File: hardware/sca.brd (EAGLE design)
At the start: 194.3 x 73.3 mm, 31 parts

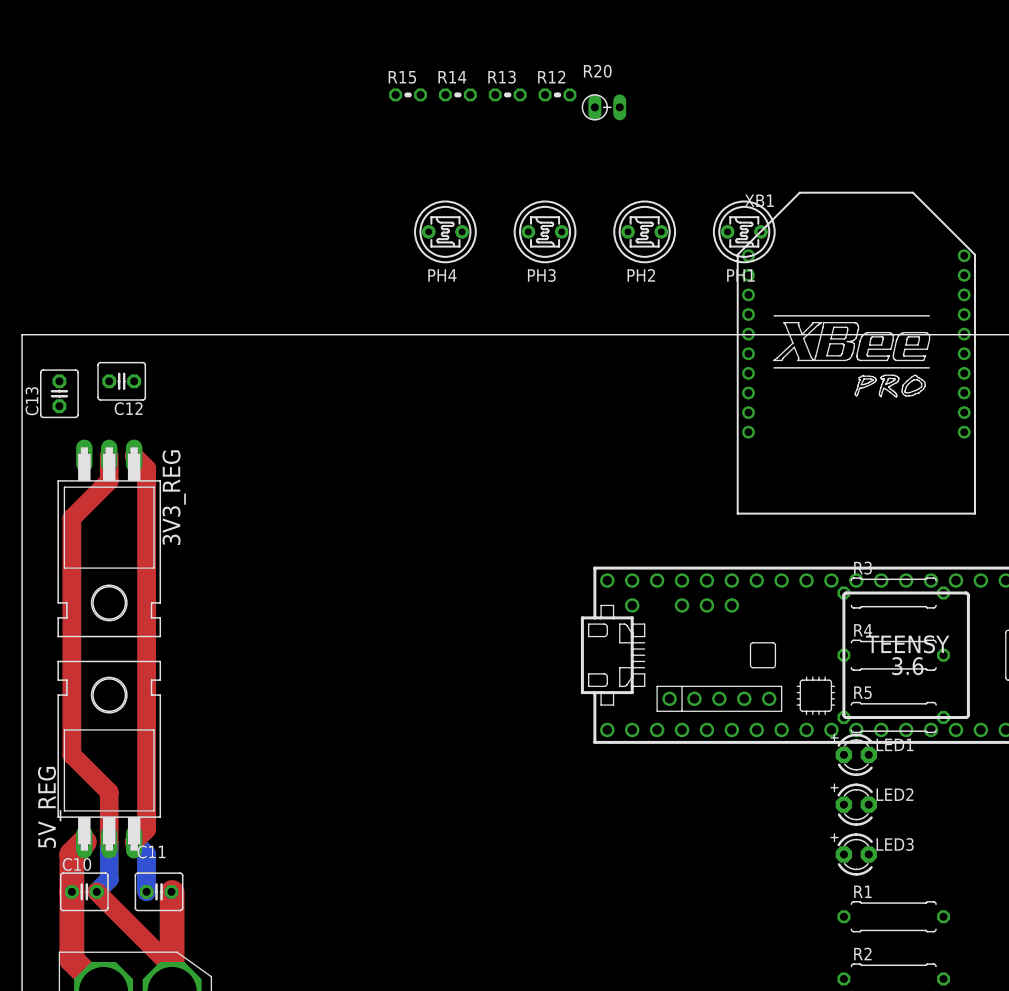
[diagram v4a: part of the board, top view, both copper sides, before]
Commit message: added thermistor routing
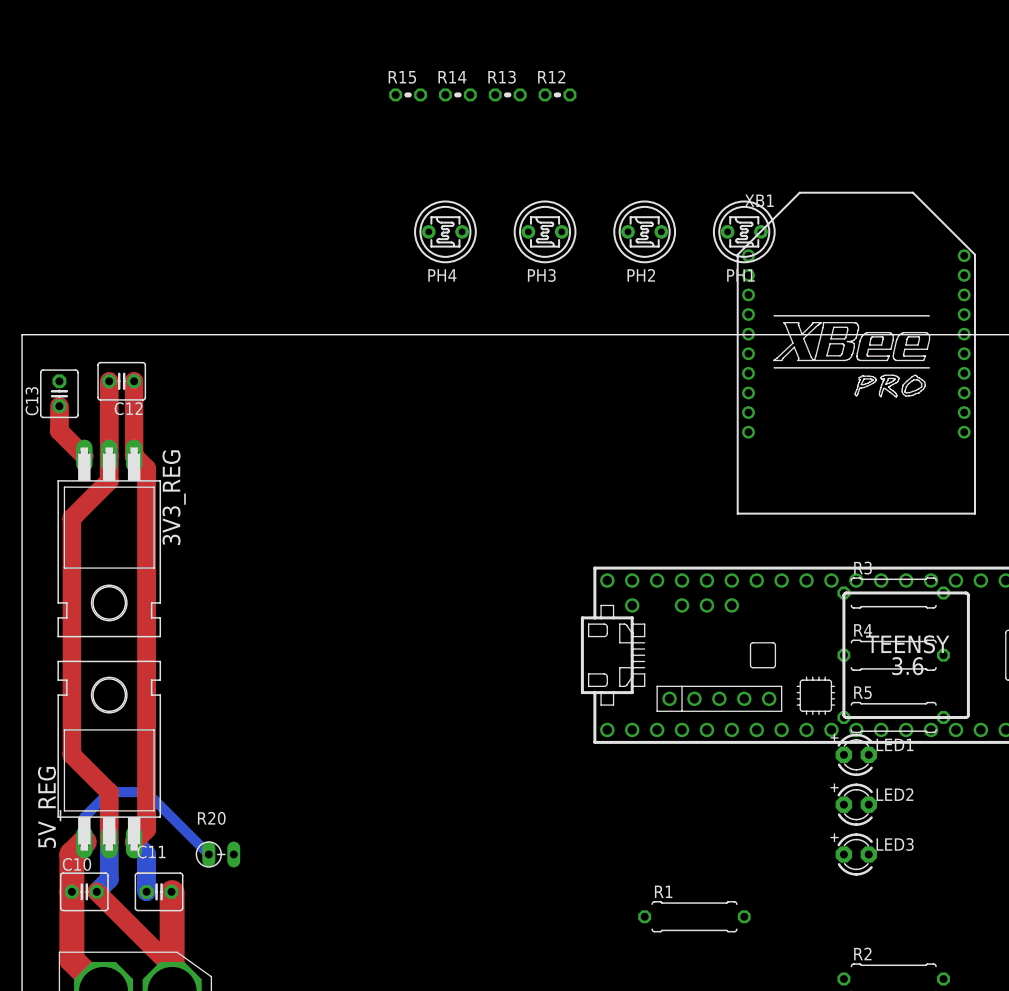
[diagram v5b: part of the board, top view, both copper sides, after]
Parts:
- moved R20 85.8 mm to (20.3, 20.3)
- moved R1 20.3 mm to (68.6, 14.0)
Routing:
- net V_BATT: track 17.1 -> 36.0 mm
- net +5V: track 46.0 -> 53.6 mm
- net GND: track 71.7 -> 79.3 mm
- net +3V3: track 0.00 -> 6.13 mm
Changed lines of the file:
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@@
 <setting verticaltext="up"/>
 </settings>
-<grid distance="50" unitdist="mil" unit="mil" style="lines" multiple="1" display="no" altdistance="5" altunitdist="mil" altunit="mil"/>
+<grid distance="50" unitdist="mil" unit="inch" style="lines" multiple="1" display="yes" altdistance="5" altunitdist="mil" altunit="mil"/>
 <layers>
 <layer number="1" name="Top" color="4" fill="1" visible="yes" active="yes"/>
@@
 <attribute name="VALUE" x="52.4764" y="106.9086" size="1.27" layer="27" ratio="12"/>
 </element>
-<element name="R20" library="varistor" library_urn="urn:adsk.eagle:library:410" package="RS-2,5" package3d_urn="urn:adsk.eagle:package:30592/1" value="THERMISTOR-2,5" x="59.69" y="96.52" smashed="yes">
-<attribute name="NAME" x="57.15" y="99.568" size="1.27" layer="25" ratio="10"/>
-<attribute name="VALUE" x="57.15" y="98.044" size="1.27" layer="27" ratio="10"/>
+<element name="R20" library="varistor" library_urn="urn:adsk.eagle:library:410" package="RS-2,5" package3d_urn="urn:adsk.eagle:package:30592/1" value="THERMISTOR-2,5" x="20.32" y="20.32" smashed="yes">
+<attribute name="NAME" x="17.78" y="23.368" size="1.27" layer="25" ratio="10"/>
+<attribute name="VALUE" x="17.78" y="21.844" size="1.27" layer="27" ratio="10"/>
 </element>
 <element name="U$1" library="Teensy356" package="TEENSY_3.5/3.6" value="TEENSY_3.5/3.6" x="87.63" y="40.64" smashed="yes"/>
@@
 <attribute name="VALUE" x="85.725" y="33.6042" size="1.27" layer="27" ratio="10"/>
 </element>
-<element name="R1" library="resistor" library_urn="urn:adsk.eagle:library:348" package="0309/10" package3d_urn="urn:adsk.eagle:package:23567/1" value="1M" x="88.9" y="13.97" smashed="yes">
-<attribute name="NAME" x="84.709" y="15.875" size="1.27" layer="25" ratio="10"/>
-<attribute name="VALUE" x="85.725" y="13.2842" size="1.27" layer="27" ratio="10"/>
+<element name="R1" library="resistor" library_urn="urn:adsk.eagle:library:348" package="0309/10" package3d_urn="urn:adsk.eagle:package:23567/1" value="1M" x="68.58" y="13.97" smashed="yes">
+<attribute name="NAME" x="64.389" y="15.875" size="1.27" layer="25" ratio="10"/>
+<attribute name="VALUE" x="65.405" y="13.2842" size="1.27" layer="27" ratio="10"/>
 </element>
 <element name="R2" library="resistor" library_urn="urn:adsk.eagle:library:348" package="0309/10" package3d_urn="urn:adsk.eagle:package:23567/1" value="1M" x="88.9" y="7.62" smashed="yes">
@@
 <wire x1="7.62" y1="16.51" x2="15.31" y2="8.82" width="1.905" layer="1"/>
 <wire x1="15.31" y1="8.82" x2="15.31" y2="6.35" width="0.1524" layer="1"/>
+<wire x1="8.89" y1="60.96" x2="8.89" y2="68.58" width="1.905" layer="1"/>
 <wire x1="143.51" y1="35.052" x2="174.625" y2="36.83" width="0" layer="19" extent="1-1"/>
 <wire x1="140.335" y1="10.16" x2="143.51" y2="35.052" width="0" layer="19" extent="1-1"/>
@@
 <wire x1="8.89" y1="68.58" x2="38.1" y2="97.79" width="0" layer="19" extent="1-1"/>
 <wire x1="3.81" y1="68.58" x2="8.89" y2="68.58" width="0" layer="19" extent="1-1"/>
-<wire x1="8.89" y1="60.96" x2="8.89" y2="68.58" width="0" layer="19" extent="1-1"/>
 </signal>
 <signal name="ENABLE">
@@
 <contactref element="JP7" pad="2"/>
 <contactref element="JP2" pad="1"/>
+<wire x1="6.35" y1="60.96" x2="3.81" y2="63.5" width="1.905" layer="1"/>
+<wire x1="3.81" y1="63.5" x2="3.81" y2="66.04" width="1.905" layer="1"/>
 <wire x1="135.255" y1="10.16" x2="172.085" y2="36.83" width="0" layer="19" extent="1-1"/>
 <wire x1="59.69" y1="48.26" x2="135.255" y2="10.16" width="0" layer="19" extent="1-1"/>
 <wire x1="74.09" y1="81.39" x2="59.69" y2="48.26" width="0" layer="19" extent="1-1"/>
 <wire x1="6.35" y1="60.96" x2="59.69" y2="48.26" width="0" layer="19" extent="1-1"/>
-<wire x1="3.81" y1="66.04" x2="6.35" y2="60.96" width="0" layer="19" extent="1-1"/>
 </signal>
 <signal name="+5V">
@@
 <wire x1="11.43" y1="21.59" x2="12.7" y2="20.32" width="1.905" layer="16"/>
 <wire x1="12.7" y1="20.32" x2="12.7" y2="16.51" width="1.905" layer="16"/>
+<wire x1="11.43" y1="60.96" x2="11.43" y2="68.58" width="1.905" layer="1"/>
 <wire x1="146.05" y1="35.052" x2="169.545" y2="36.83" width="0" layer="19" extent="1-1"/>
 <wire x1="71.96" y1="83.82" x2="146.05" y2="35.052" width="0" layer="19" extent="1-1"/>
@@
 <wire x1="41.48" y1="83.82" x2="51.64" y2="83.82" width="0" layer="19" extent="1-1"/>
 <wire x1="11.43" y1="68.58" x2="41.48" y2="83.82" width="0" layer="19" extent="1-1"/>
-<wire x1="11.43" y1="60.96" x2="11.43" y2="68.58" width="0" layer="19" extent="1-1"/>
 </signal>
 <signal name="V_BATT">
@@
 <wire x1="6.35" y1="21.59" x2="5.08" y2="20.32" width="2.54" layer="1"/>
 <wire x1="5.08" y1="20.32" x2="5.08" y2="16.51" width="2.54" layer="1"/>
-<wire x1="93.98" y1="13.97" x2="58.42" y2="96.52" width="0" layer="19" extent="1-1"/>
-<wire x1="8.31" y1="6.35" x2="93.98" y2="13.97" width="0" layer="19" extent="1-1"/>
+<wire x1="19.05" y1="20.32" x2="12.7" y2="26.67" width="1.016" layer="16"/>
+<wire x1="8.89" y1="26.67" x2="6.35" y2="24.13" width="1.016" layer="16"/>
+<wire x1="6.35" y1="24.13" x2="6.35" y2="21.59" width="1.016" layer="16"/>
+<wire x1="12.7" y1="26.67" x2="8.89" y2="26.67" width="1.016" layer="16"/>
+<wire x1="19.05" y1="20.32" x2="73.66" y2="13.97" width="0" layer="19" extent="1-1"/>
 </signal>
 <signal name="CS">
@@
 <contactref element="R20" pad="2"/>
 <contactref element="U$1" pad="A10"/>
-<wire x1="60.96" y1="96.52" x2="53.34" y2="109.22" width="0" layer="19" extent="1-1"/>
-<wire x1="69.85" y1="45.72" x2="60.96" y2="96.52" width="0" layer="19" extent="1-1"/>
+<wire x1="69.85" y1="45.72" x2="53.34" y2="109.22" width="0" layer="19" extent="1-1"/>
+<wire x1="21.59" y1="20.32" x2="69.85" y2="45.72" width="0" layer="19" extent="1-1"/>
 </signal>
 <signal name="SDI/SDA">
@@
 <contactref element="R2" pad="1"/>
 <contactref element="U$1" pad="2"/>
-<wire x1="83.82" y1="13.97" x2="67.31" y2="33.02" width="0" layer="19" extent="1-1"/>
-<wire x1="83.82" y1="7.62" x2="83.82" y2="13.97" width="0" layer="19" extent="1-1"/>
+<wire x1="63.5" y1="13.97" x2="67.31" y2="33.02" width="0" layer="19" extent="1-1"/>
+<wire x1="83.82" y1="7.62" x2="63.5" y2="13.97" width="0" layer="19" extent="1-1"/>
 </signal>
 <signal name="N$1">

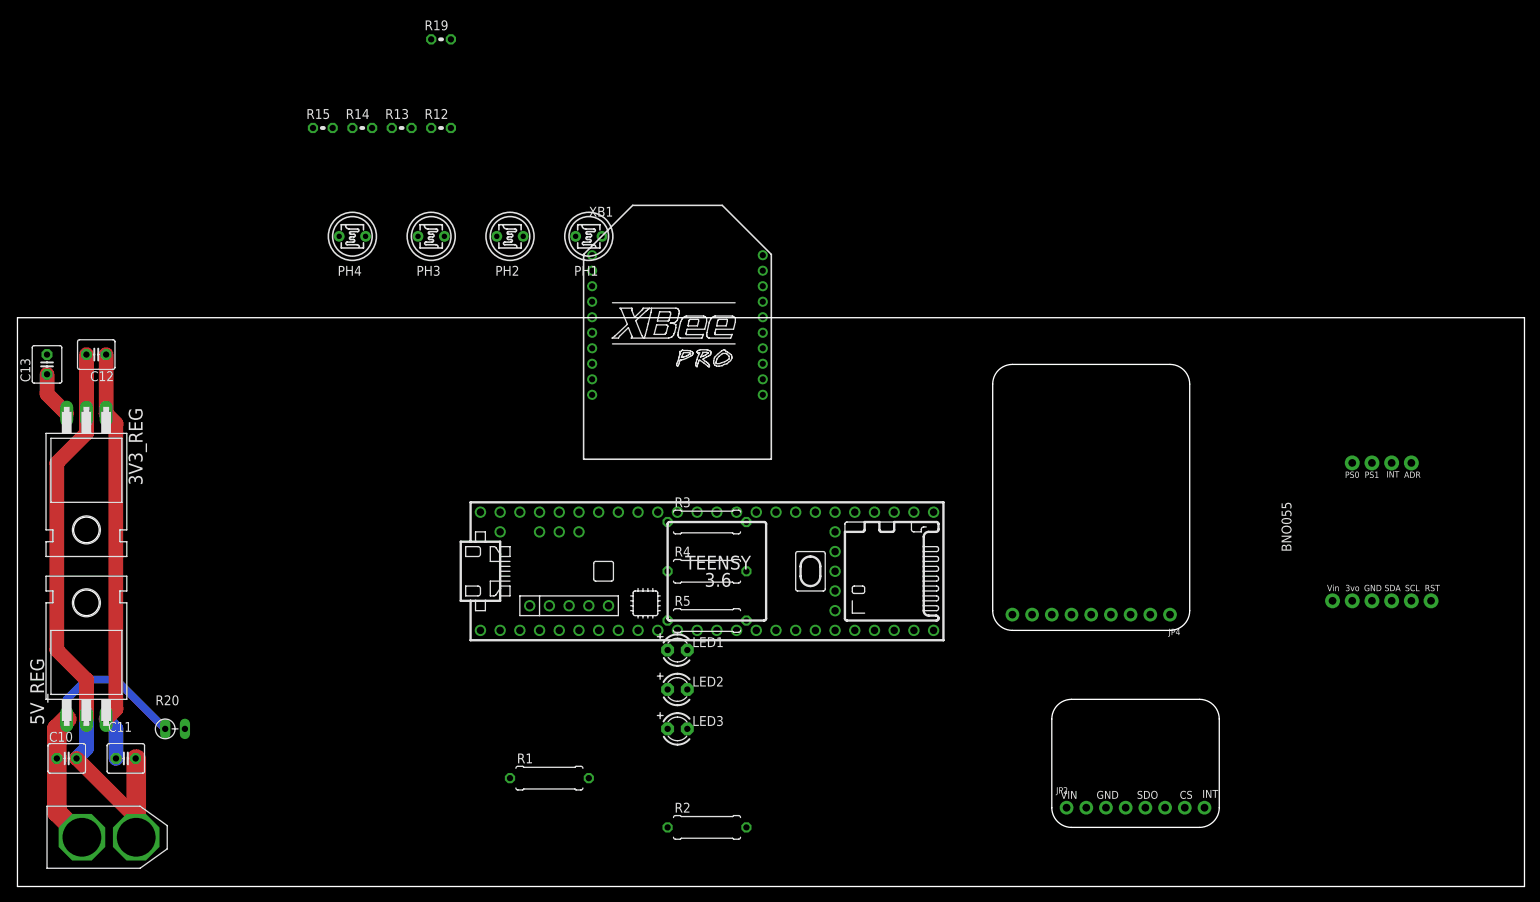
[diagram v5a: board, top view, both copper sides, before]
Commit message: lots of layout changes
updated teensy footprint to get rid of internal pins and pads
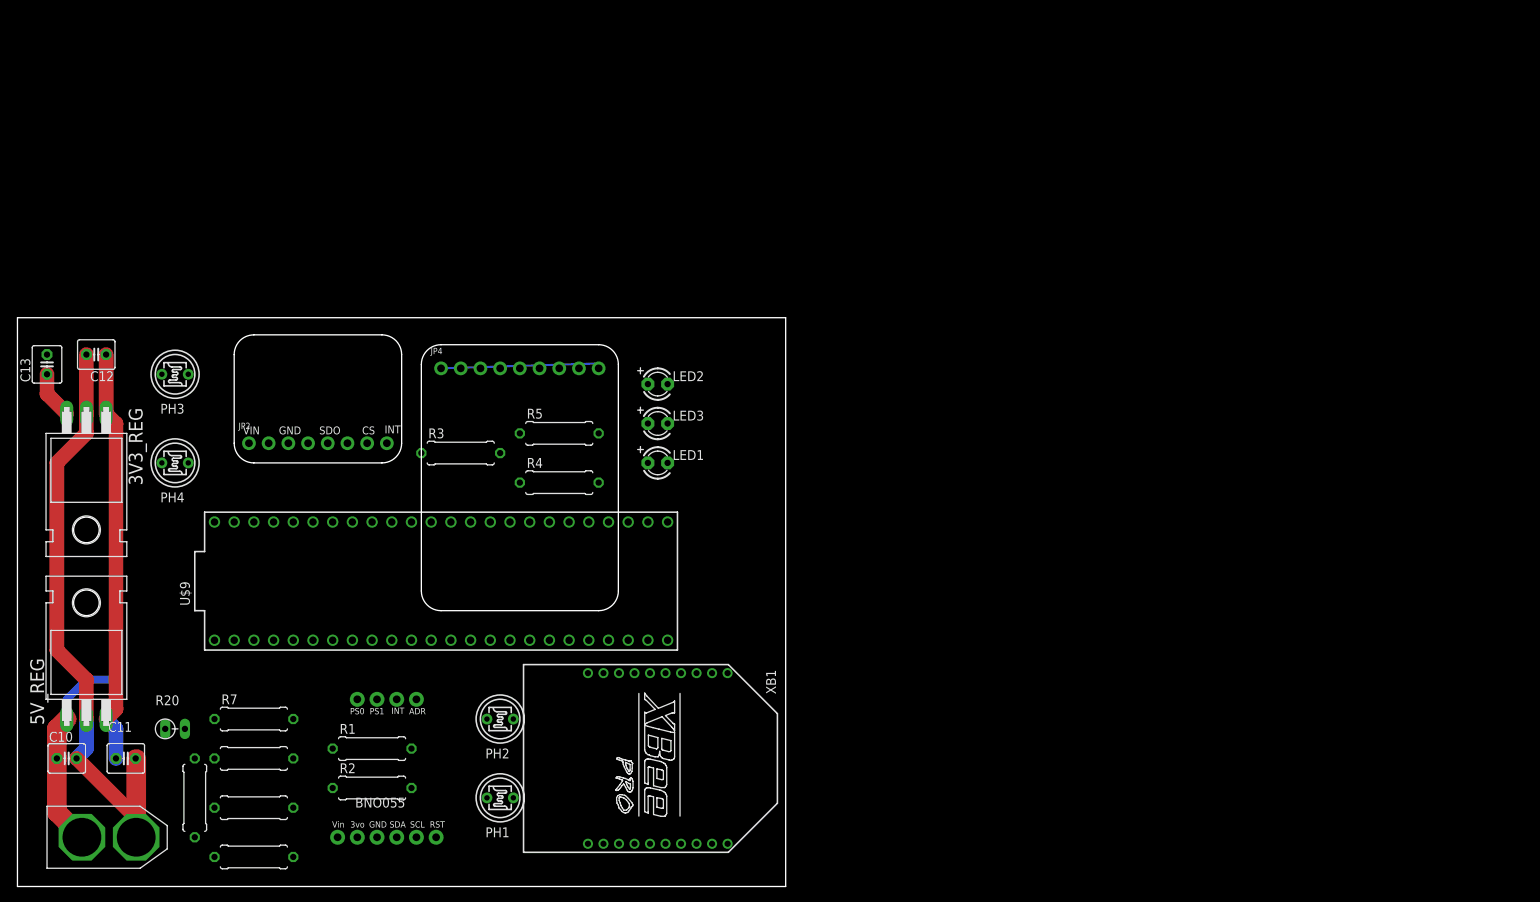
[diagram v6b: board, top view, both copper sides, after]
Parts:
- removed R12, R13, R14, R15: 10k, adafruit:0204V
- removed R19: (no value), adafruit:0204V
- removed U$1: TEENSY_3.5/3.6, Teensy356:TEENSY_3.5/3.6
- added R10, R6, R7, R8, R9: 1M, resistor:0309/10
- added U$9: TEENSY_3.6_DIL, Teensy_3_and_LC_Series_Boards_v1.4:TEENSY_3.6_DIL
- moved JP7 131.8 mm to (47.6, 6.35)
- moved JP8 131.8 mm to (47.6, 24.1)
- moved JP2 115.4 mm to (38.7, 57.1)
- moved JP4 80.2 mm to (64.8, 66.8), turned to 0 degrees
- moved PH1 73.3 mm to (62.2, 11.4)
- moved PH2 62.2 mm to (62.2, 21.6)
- moved XB1 55.9 mm to (82.5, 16.5), turned to 270 degrees
- moved R2 43.5 mm to (45.7, 12.7)
- moved LED2 39.5 mm to (82.5, 64.8)
- moved LED3 39.5 mm to (82.5, 59.7)
- moved PH3 37.5 mm to (20.3, 66.0)
- moved PH4 37.1 mm to (20.3, 54.6)
- moved R3 33.0 mm to (57.1, 55.9)
- moved R5 30.7 mm to (69.8, 58.4)
- moved LED1 24.3 mm to (82.5, 54.6)
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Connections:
- removed net N$1: U$1.0/RX, XB1.2
- removed net N$14: R5.1, U$1.30
- removed net N$15: PH3.2, R14.2, U$1.16/A2
- removed net N$16: R4.1, U$1.29
- removed net N$17: R3.1, U$1.28
- removed net N$18: R1.1, R2.1, U$1.2
- removed net N$19: PH4.2, R15.2, U$1.17/A3
- removed net N$2: PH2.2, R13.2, U$1.15/A1
- removed net N$4: U$1.1/TX, XB1.3
- removed net N$6: PH1.2, R12.2, U$1.14/A0
- removed net N$9: R19.1, R20.2, U$1.A10
- removed net RX: JP4.4, U$1.10/CS
- removed net SCK/SCL: JP2.4, JP7.5, U$1.19/A5/SCL
- removed net SDI/SDA: JP2.6, JP7.4, U$1.18/A4/SDA
- removed net TX: JP4.5, U$1.9/CS
- new net 3.3V: U$9.3.3V, U$9.3.3V3
- new net AGND: U$9.AGND
- new net BATT_T: R10.2, R20.2, U$9.3
- new net GPS_RX: JP4.4, U$9.10
- new net GPS_TX: JP4.5, U$9.9
- new net LED_1: R3.1, U$9.28
- new net LED_2: R4.1, U$9.29
- new net LED_3: R5.1, U$9.30
- new net MCU_2: R1.1, R2.1, U$9.2
- new net MCU_RX: U$9.0, XB1.2
- new net MCU_TX: U$9.1, XB1.3
- new net PR_1: PH1.2, R7.2, U$9.14/A0
- new net PR_2: PH2.2, R6.1, U$9.15/A1
- new net PR_3: PH3.2, R8.1, U$9.16/A2
- new net PR_4: PH4.2, R9.1, U$9.17/A3
- new net SCL: JP2.4, JP7.5, U$9.37/A18
- new net SDA: JP2.6, JP7.4, U$9.38/A19
- net +3V3: now also PH1.1, PH2.1, PH3.1, PH4.1, R20.1, U$9.VIN; no longer U$1.VIN
- net +5V: no longer PH1.1, PH2.1, PH3.1, PH4.1
- net GND: now also R10.1, R6.2, R7.1, R8.2, R9.2, U$9.GND, U$9.GND1; no longer R12.1, R13.1, R14.1, R15.1, R19.2, U$1.GND
- net V_BATT: no longer R20.1
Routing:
- net 1PPS: track 0.63 -> 20.3 mm
- net V_BATT: track 36.0 -> 27.0 mm
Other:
- board size 194.3 x 73.3 mm -> 99 x 73.3 mm
